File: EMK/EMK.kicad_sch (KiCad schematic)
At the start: 50 parts, among them J1 USB_C_Receptacle_USB2.0_14P, J2 Conn_01x02_Socket, J3 Conn_ARM_JTAG_SWD_10, Q1 Si2371EDS, SW1 SW_Nidec_CAS-120A1, SW18 SW_Push, U1 nRF52840-QFAA, U2 15nH, U3 TPS62822DLC, U4 USBLC6-2SC6, U5 TP4057, Y1 Crystal_32.768kHz, Y2 Crystal_32mHz

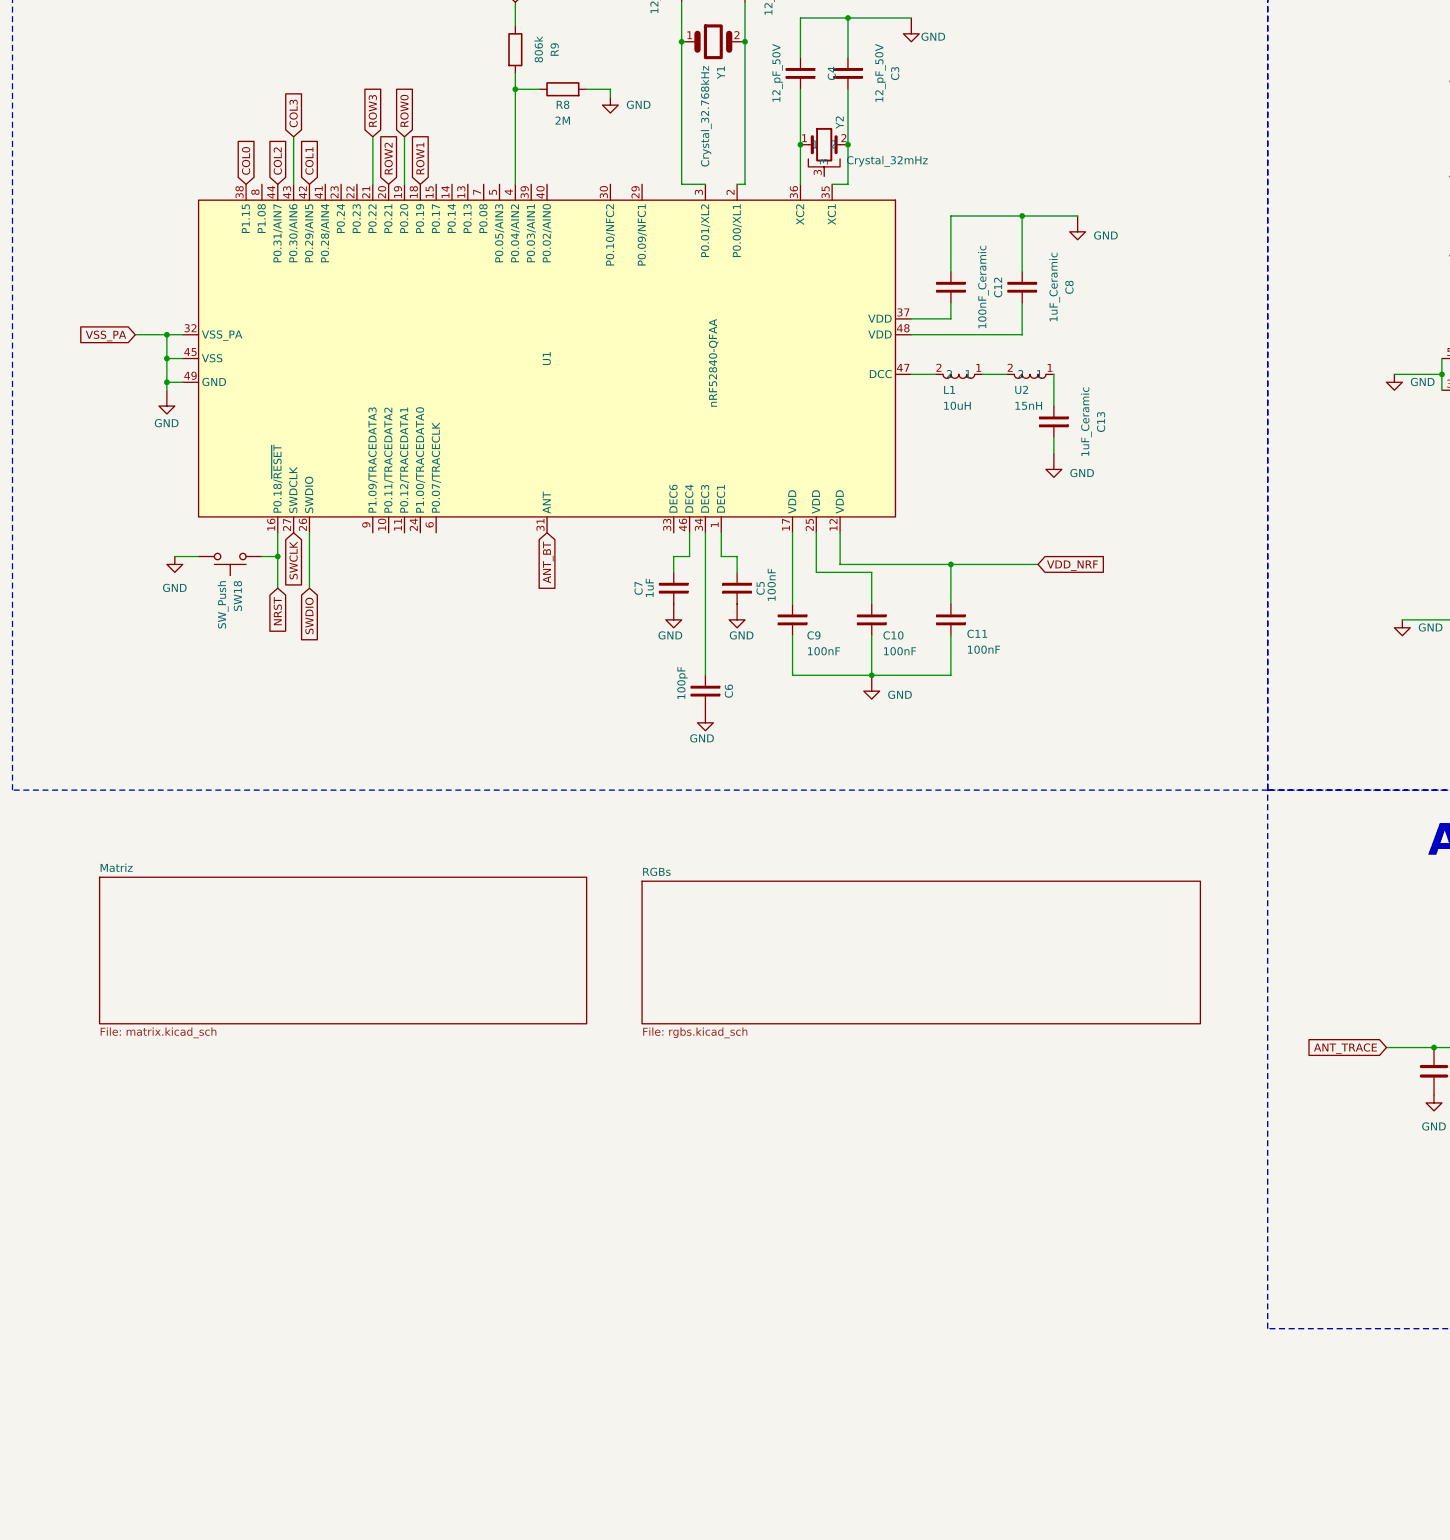
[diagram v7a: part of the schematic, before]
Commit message: feat: adiciona o controle de alimentação dos RGBs.
Signed-off-by: Paulo Santos <prms@ic.ufal.br>
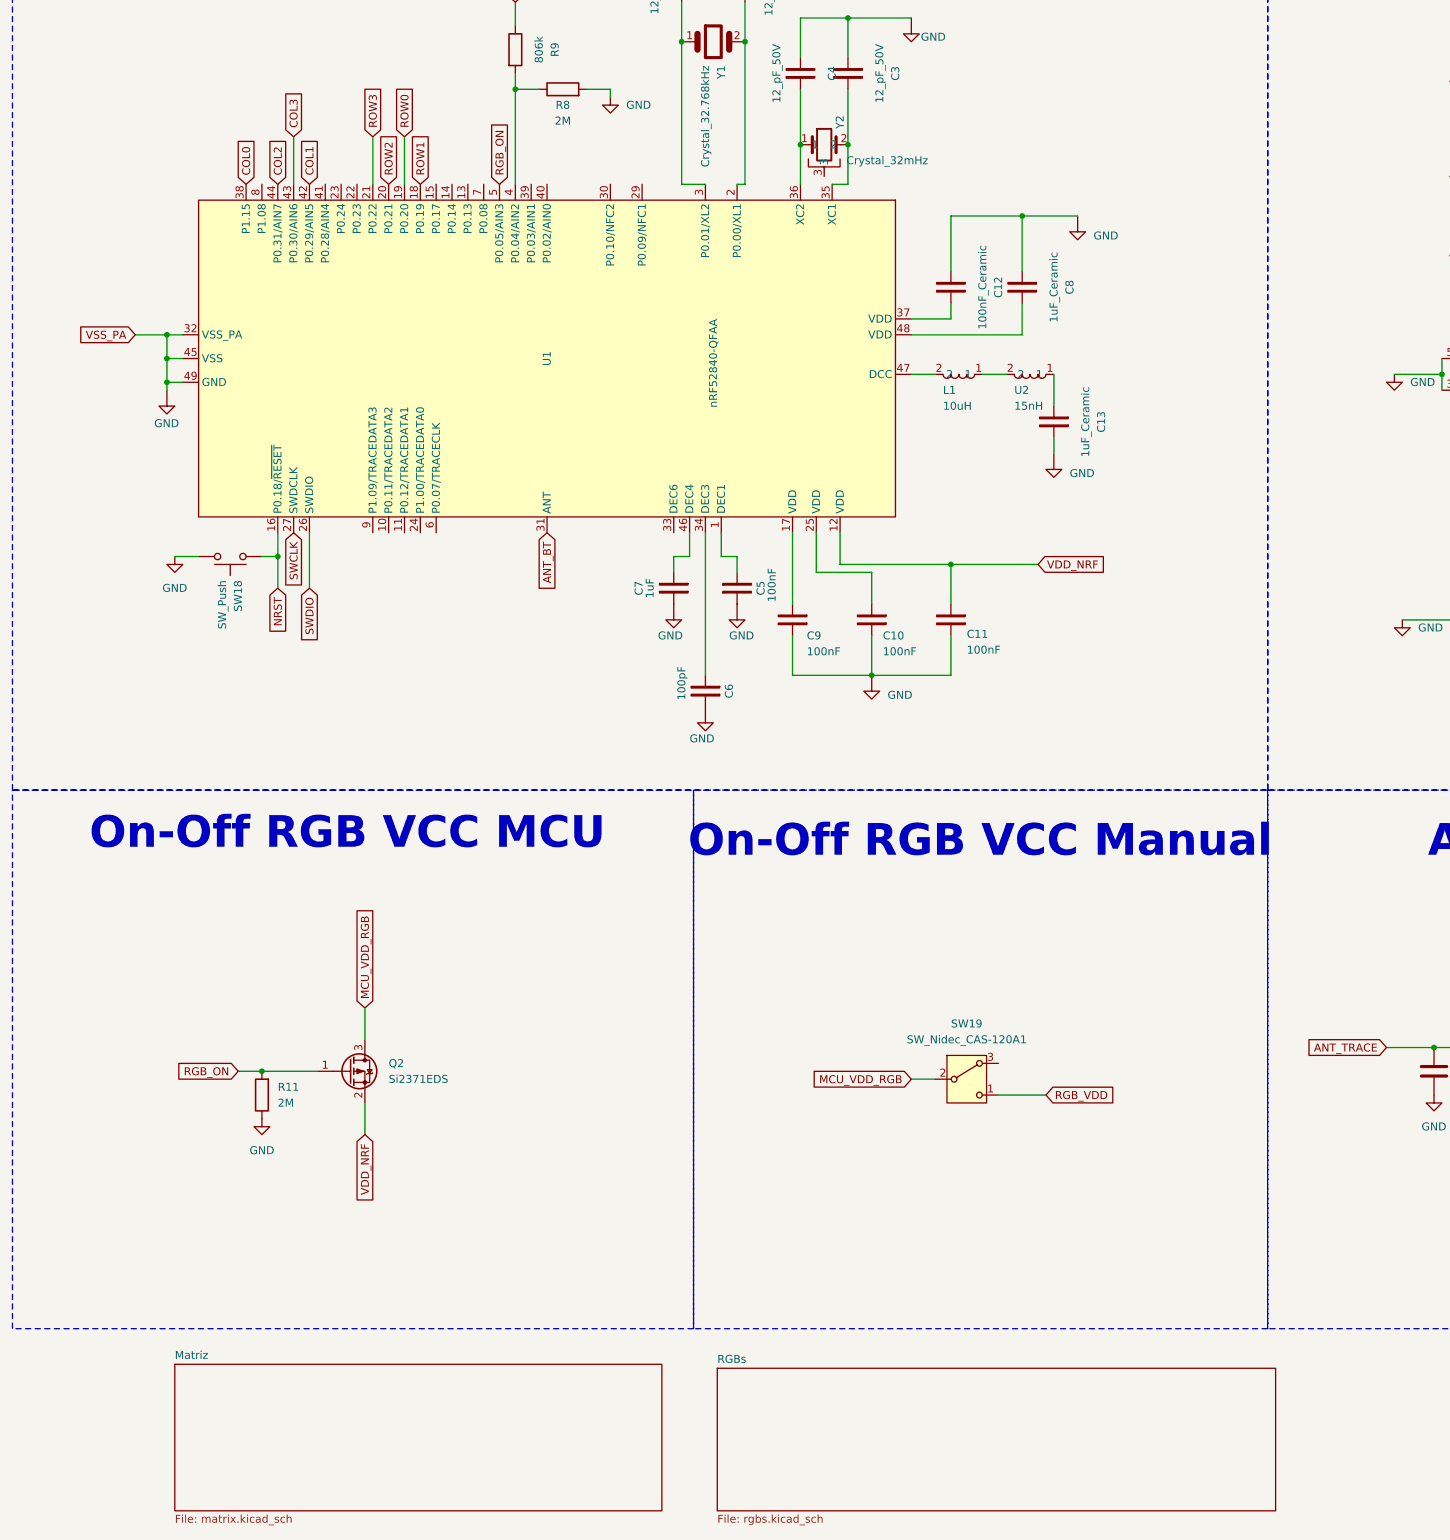
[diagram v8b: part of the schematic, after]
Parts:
- added Q2: Si2371EDS, Package_TO_SOT_SMD:SOT-23, symbol EMKPower:Si2371EDS
- added R11: 2M, symbol Device:R
- added SW19: SW_Nidec_CAS-120A1, Button_Switch_SMD:Nidec_Copal_CAS-120A, symbol Switch:SW_Nidec_CAS-120A1
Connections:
- net GND: now also R11.1
- net VDD_NRF: now also Q2.2 (S)
- net RGB_ON: now reaches U1.5 (P0.05/AIN3)
- net RGB_ON: now also Q2.1 (G), R11.2
- new net MCU_VDD_RGB: Q2.3 (D), SW19.2 (B)
- new net RGB_VDD: SW19.1 (C)
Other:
- note added: "On-Off RGB VCC MCU"
- note added: "On-Off RGB VCC Manual"
